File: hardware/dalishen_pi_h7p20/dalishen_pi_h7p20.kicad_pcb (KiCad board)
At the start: 4 copper layers, 92 x 64 mm, 227 parts, among them J1 Conn_02x05_Odd_Even, J10 RJ45_HR911130A, J1001 USB_C_Receptacle_USB2.0_16P, J2 USB_C_Receptacle_USB2.0_16P, J3 USB_A, J6 5V, J7 OV5640, J9 D500C930SV0, SW1 SW_Push, SW2 SW_Push, SW3 SW_DIP_x03, U1 YT8531C, U1001 AIC8800FC, U1002 P25Q80H/P25Q64H/P25Q128HA, U18 LM2903A-VR, U19 LM2903A-VR, U2 LM2903A-VR, U20 USB3343, U3 H7P20N0L128-M3H1, U4 SY7201ABC, U5 XC6206-2.8, U6 EA3036C, U7 P25Q32SH-SSH-IT, U8 XC6206-1.5, U9 CJ3439KDW, Y1 26M, Y1001 26M, 10PPM, Y2 25M, 10PPM

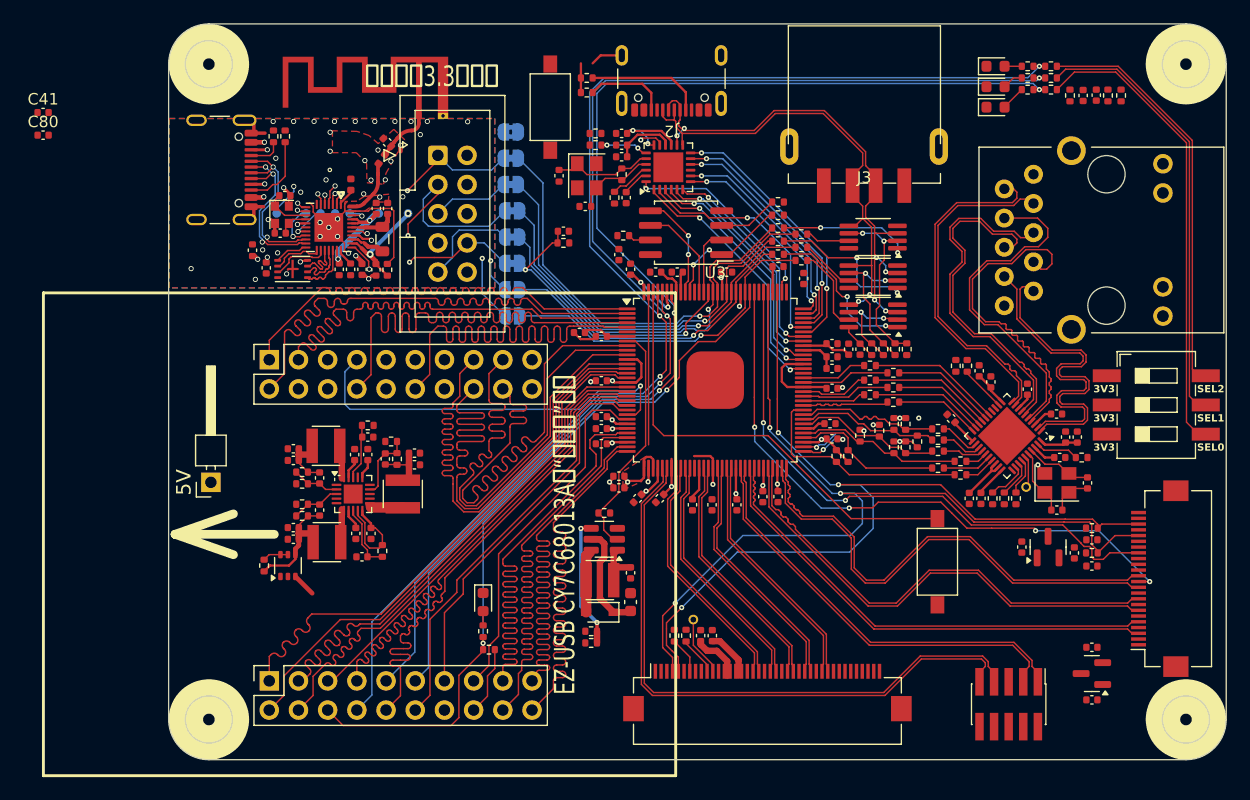
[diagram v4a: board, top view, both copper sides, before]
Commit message: [dalishen_pi_h7p20] 原理图初稿
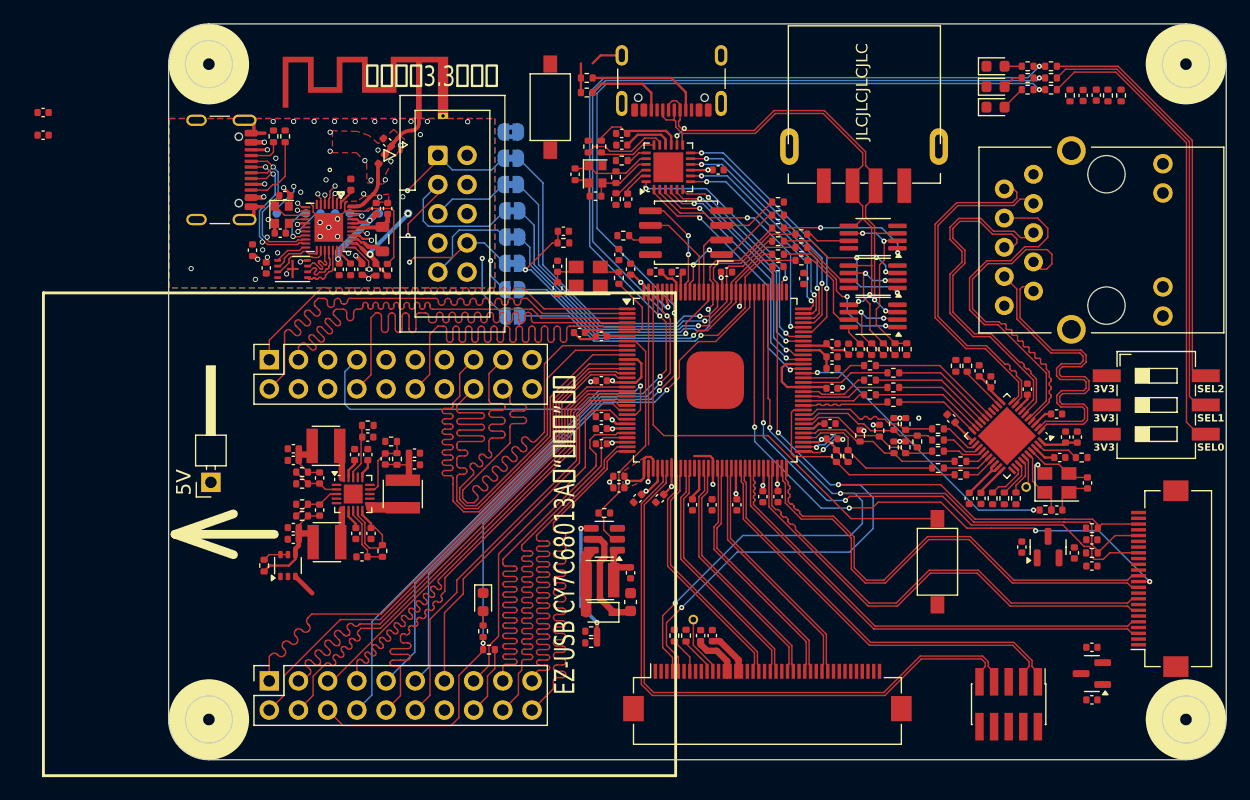
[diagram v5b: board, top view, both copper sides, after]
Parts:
- added C2: NC, Capacitor_SMD:C_0402_1005Metric, F.Cu at (142.5, 110.7)
- added R4: 0, Resistor_SMD:R_0402_1005Metric, F.Cu at (146.3, 100.3)
- added R6: 0, Resistor_SMD:R_0402_1005Metric, F.Cu at (184.9, 132.0)
- added R7: NC, Resistor_SMD:R_0402_1005Metric, F.Cu at (142.5, 112.6)
- added R8: 33, Resistor_SMD:R_0402_1005Metric, F.Cu at (147.8, 111.8)
- added X1: NC, vllogic:OSC_3225, F.Cu at (145.2, 111.6)
- C78, C79: value 12pF -> NC
- R29, R31, R35: value 10k,1% -> 20k,1%
- R30, R34: value 10k,1% -> 33k,1%
- R33: value 10k,1% -> 150k,1%
- R36: value 33k -> 33k,1%
- Y1: footprint vllogic:OSC_3225 -> vllogic:OSC_2016
- Y2: value 25M, 10PPM -> NC
- moved C15 8.67 mm to (156.5, 102.4), turned to 180 degrees
- moved R89 2.65 mm to (148.1, 101.5)
- moved C12 1.40 mm to (144.0, 102.7)
- moved R79 1.31 mm to (145.2, 100.3), turned to -90 degrees
- moved C14 1.26 mm to (145.8, 104.6)
- moved C13 1.02 mm to (148.1, 100.2)
- moved Y1 0.77 mm to (145.8, 102.7)
- moved R78 0.57 mm to (147.6, 103.0)
- moved C49 0.18 mm to (148.6, 104.9)
- moved R90 0.18 mm to (147.6, 104.9)
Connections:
- net /ET3036C/EA3036_EN2 renamed /ET3036C_CJ3439KDW/EA3036_EN2
- net /ET3036C/EA3036_EN3 renamed /ET3036C_CJ3439KDW/EA3036_EN3
- C50 pad 2: Net-(U20-ID) -> Net-(U20-VDD33)
- U20 pad 15: Net-(U20-ID) -> Net-(U20-VDD33)
- U3 pad 6: unconnected-(U3-IO13_PCLK_8-Pad6) -> Net-(U3-IO13_PCLK_8)
- U3 pad 82: unconnected-(U3-IO3_3-Pad82) -> /FPGA_ETHA_25M
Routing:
- net /FPGA_ETHA_25M: track 0.00 -> 25.5 mm, vias 0 -> 2
- net Net-(U20-VDD33): track 0.00 -> 8.01 mm
- net Net-(U3-IO13_PCLK_8): track 0.00 -> 6.12 mm
- net Net-(U20-VBUS): track 2.12 -> 7.48 mm, vias 1 -> 0
- net /VCC_3V3: track 59.3 -> 63.0 mm, vias 9 -> 10
- net GND: track 37.2 -> 39.6 mm
- net Net-(U20-RBIAS): track 4.17 -> 1.88 mm, vias 2 -> 0
- net Net-(U20-ID): track 7.32 -> 5.12 mm, vias 2 -> 0
- net Net-(X1-EN): track 0.00 -> 1.91 mm
- net Net-(X1-OUT): track 0.00 -> 1.80 mm
- net Net-(U20-XO): track 8.83 -> 7.21 mm
- net Net-(U20-REFCLK/XI): track 7.13 -> 5.65 mm
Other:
- board text added: "JLCJLCJLCJLC"

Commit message: [dalishen_pi_h7p20] 原理图预审
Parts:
- C1002: value 1.3pF -> NC
- C1011: value 10uF -> NC
- C12, C14: value 9pF -> 4.3pF
- C69: value 1uF/35V -> 1uF,50V
- L1001: value 1.4nH -> 0R
- L1003: value 1.8nH -> 0R
- moved C41 67.0 mm to (154.2, 133.4), turned to 90 degrees
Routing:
- net /VDD_CORE: track 30.1 -> 32.5 mm

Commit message: [dalishen_pi_h7p20] 原理图预审
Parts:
- removed C80: NC, Capacitor_SMD:C_0402_1005Metric
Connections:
- C70 pad 2: /VDDIO_1V8 -> /VCC_3V3
- J9 pad 15: /VDDIO_1V8 -> /VCC_3V3
- J9 pad 16: /VDDIO_1V8 -> /VCC_3V3
- R21 pad 2: /VDDIO_1V8 -> /VCC_3V3
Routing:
- net /VCC_3V3: track 63.0 -> 68.4 mm
- net /VDDIO_1V8: track 21.9 -> 17.5 mm

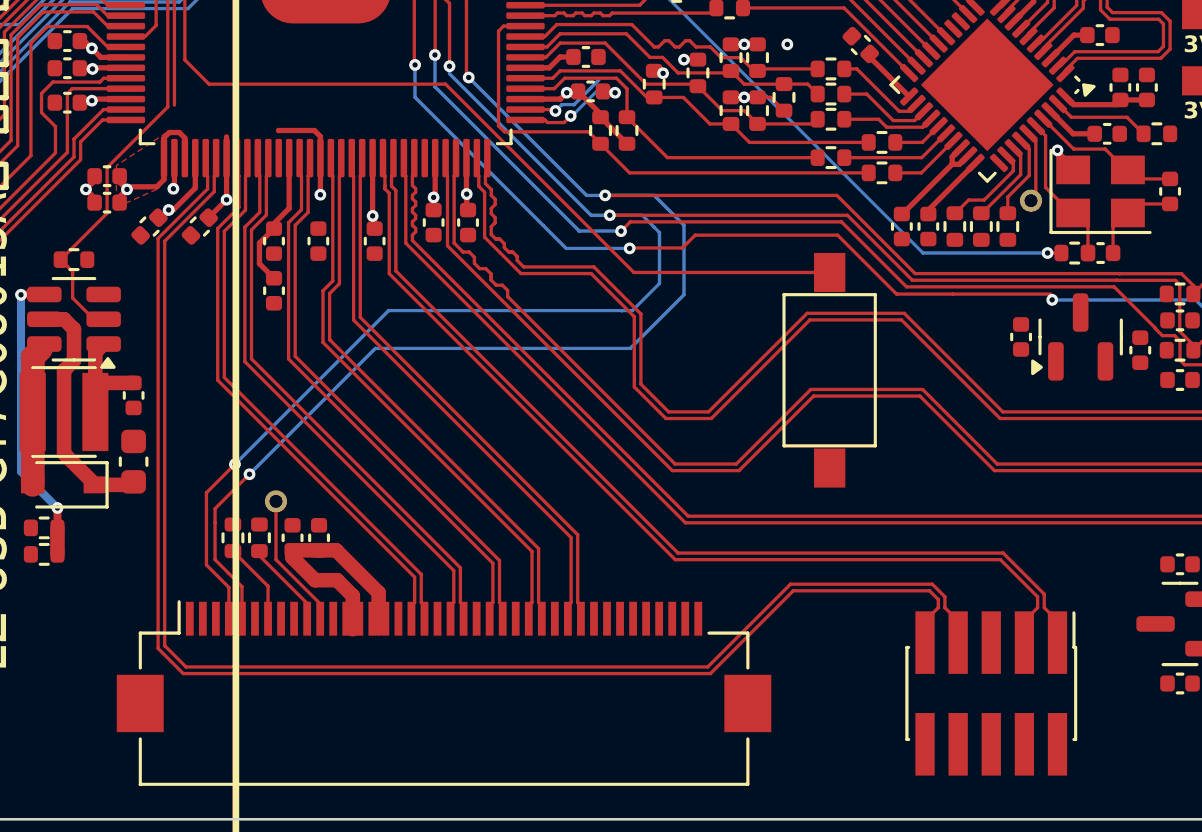
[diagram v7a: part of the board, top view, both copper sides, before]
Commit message: [dalishen_pi_h7p20] CRST电容增大、MIPI CSI使用同一bank
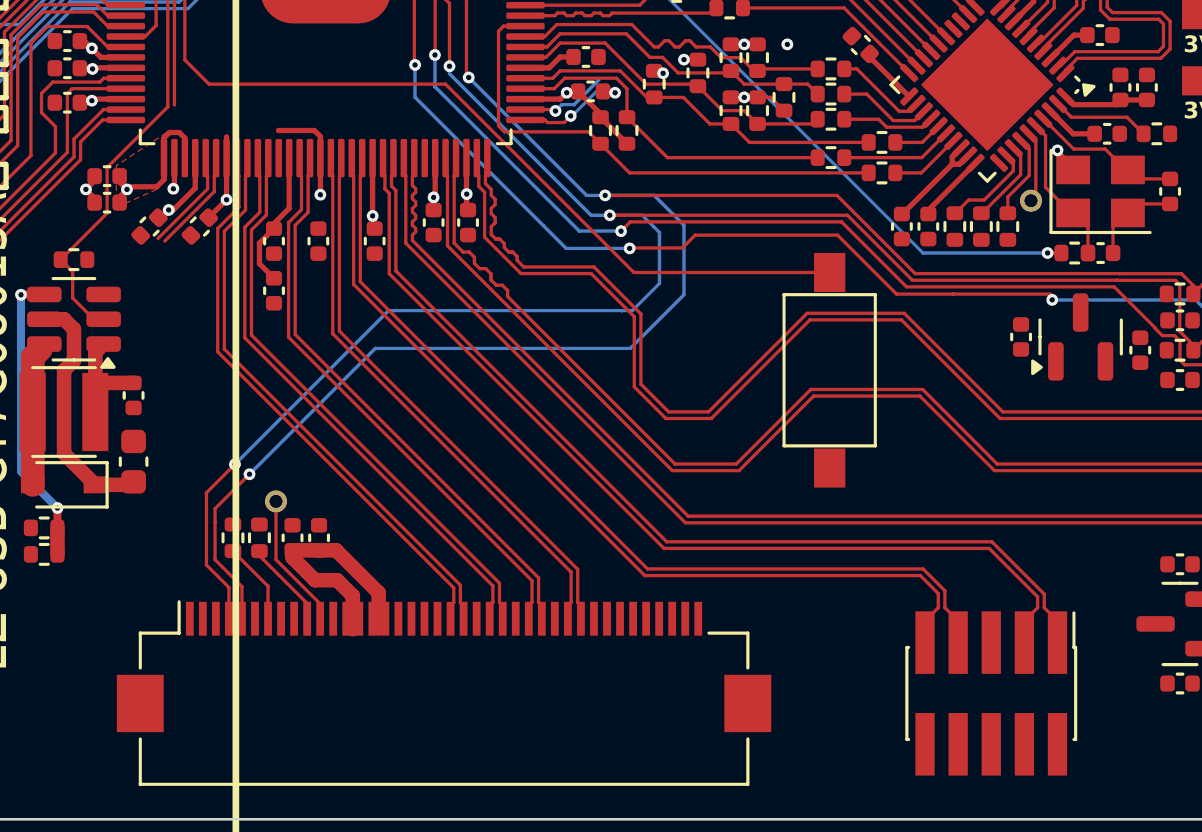
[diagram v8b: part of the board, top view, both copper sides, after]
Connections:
- J1 pad 7: /B10_IO2P -> /B9_IO2P
- J1 pad 9: /B10_IO2N -> /B9_IO2N
- J9 pad 18: /B10_IO4N -> /B10_IO2N
- J9 pad 19: /B10_IO4P -> /B10_IO2P
- J9 pad 21: /B10_IO6N -> /B10_IO4N
- J9 pad 22: /B10_IO6P -> /B10_IO4P
- J9 pad 24: /B10_IO9N -> /B10_IO6N
- J9 pad 25: /B10_IO9P -> /B10_IO6P
- J9 pad 27: /B10_IO12N -> /B10_IO9N
- J9 pad 28: /B10_IO12P -> /B10_IO9P
- J9 pad 30: /B9_IO2N -> /B10_IO12N
- J9 pad 31: /B9_IO2P -> /B10_IO12P
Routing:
- net /B10_IO2N: track 53.3 -> 3.90 mm
- net /B10_IO2P: track 53.3 -> 4.00 mm
- net /B9_IO2P: track 21.2 -> 34.3 mm
- net /B9_IO2N: track 21.2 -> 34.3 mm
- net /B10_IO6P: track 21.3 -> 21.9 mm
- net /B10_IO6N: track 21.3 -> 21.9 mm
- net /B10_IO9P: track 21.2 -> 21.8 mm
- net /B10_IO9N: track 21.2 -> 21.8 mm
- net /B10_IO4P: track 21.2 -> 21.8 mm
- net /B10_IO4N: track 21.2 -> 21.8 mm
